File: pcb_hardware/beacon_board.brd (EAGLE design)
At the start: 100 x 38.1 mm, 66 parts, among them IC1-AVR ATMEGA32U4TQFP, J1-ISP AVR_SPI_PRG_6PTH, Q1 PZT2222A, Q2 PZT2222A, Q3 PZT2222A, Q4 PZT2222A, Q5 PZT2222A, Q6 PZT2222A, Q7 PZT2222A, Y1 16MHz

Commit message: Complete alpha prototype for PCB
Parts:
- removed FRAME1: FRAME-LETTER, SparkFun-Aesthetics:CREATIVE_COMMONS
- added R11, R30, R31, R32: 1K, SparkFun-Passives:0805
- moved R5 169.3 mm to (76.2, 12.7), turned to 270 degrees
- moved R4 143.4 mm to (58.4, 29.2)
- moved R3 139.7 mm to (50.8, 11.4), turned to 90 degrees
- moved R2 138.6 mm to (53.3, 11.4), turned to 90 degrees
- moved J1-ISP 129.5 mm to (73.7, 5.08), turned to 180 degrees
- moved C1 129.0 mm to (66.0, 12.7)
- moved C3 127.6 mm to (63.5, 26.7)
- moved JP2-RESET 126.5 mm to (64.8, 3.81), turned to 270 degrees
- moved C5 126.3 mm to (47.0, 11.4)
- moved C2 125.2 mm to (57.1, 11.4)
- moved R1 124.1 mm to (48.3, 26.7), turned to 180 degrees
- moved LOGO1 119.9 mm to (71.1, 34.9)
- moved C4 118.8 mm to (45.7, 17.8), turned to 90 degrees
- moved R27 110.8 mm to (76.2, 34.3), turned to 90 degrees
- moved U$1 90.4 mm to (42.5, 32.8)
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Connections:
- new net N$30: R11.2, R30.2, R31.2, R32.2
- new net N$31: R11.1, R30.1, R31.1, R32.1
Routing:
- net VCC: track 0.00 -> 267.4 mm
- net GND: track 0.00 -> 241.3 mm, vias 0 -> 3
- net N$25: track 0.00 -> 63.0 mm
- net GREEN: track 0.00 -> 58.5 mm
- net N$15: track 0.00 -> 53.6 mm
- net WHITE: track 0.00 -> 35.1 mm
- net D9: track 0.00 -> 34.3 mm
- net D1: track 0.00 -> 34.3 mm
- net RESET: track 0.00 -> 34.2 mm, vias 0 -> 2
- net IR_RX: track 0.00 -> 34.0 mm
- net 38_KHZ_OUT: track 0.00 -> 32.9 mm
- net N$6: track 0.00 -> 32.7 mm
- net D2: track 0.00 -> 31.5 mm
- net MOSI: track 0.00 -> 30.6 mm, vias 0 -> 1
- net N$14: track 0.00 -> 23.4 mm
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- added copper zone on layer 16, net GND
- added copper zone on layer 1, net VCC
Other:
- board text added: "Green"
- board text added: "Junior Design Beacon Board"
- board text added: "R0-8-20-KT"
- board text added: "Red"
- board text added: "White"

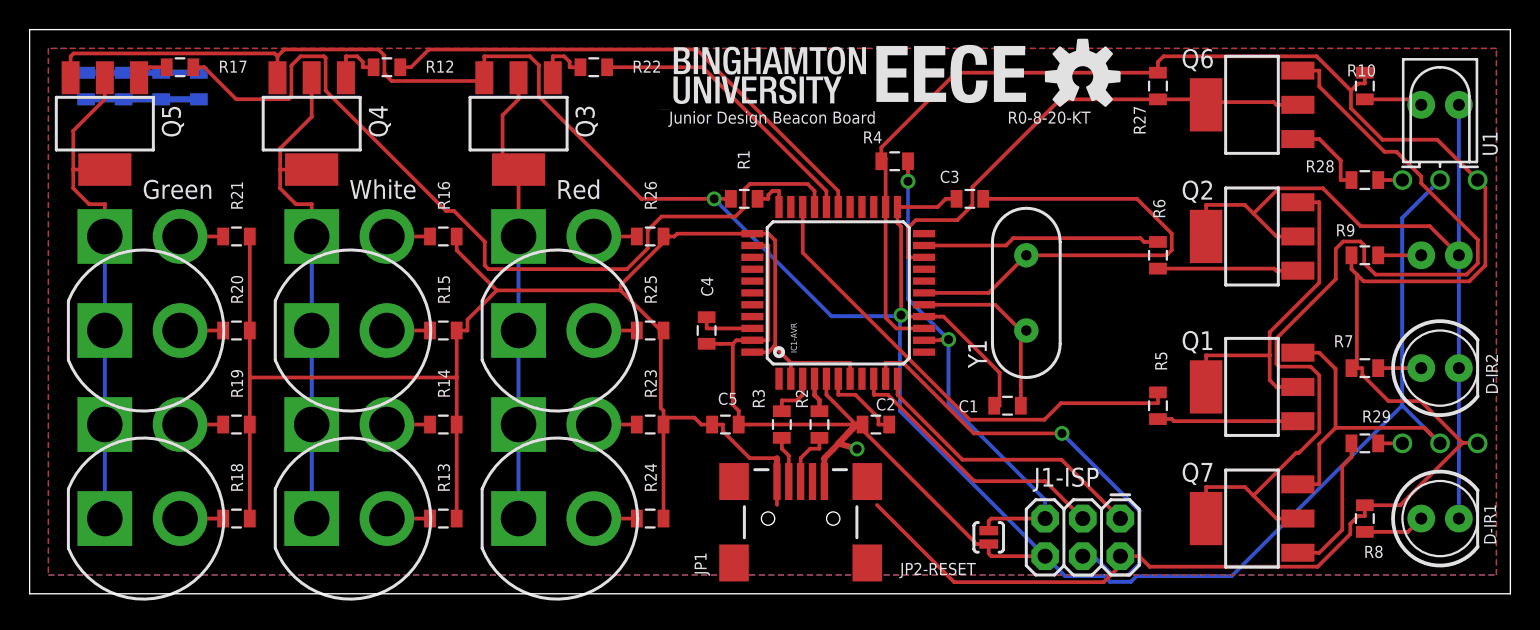
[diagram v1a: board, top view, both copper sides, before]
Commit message: Finish R1 of the beacon board PCB.
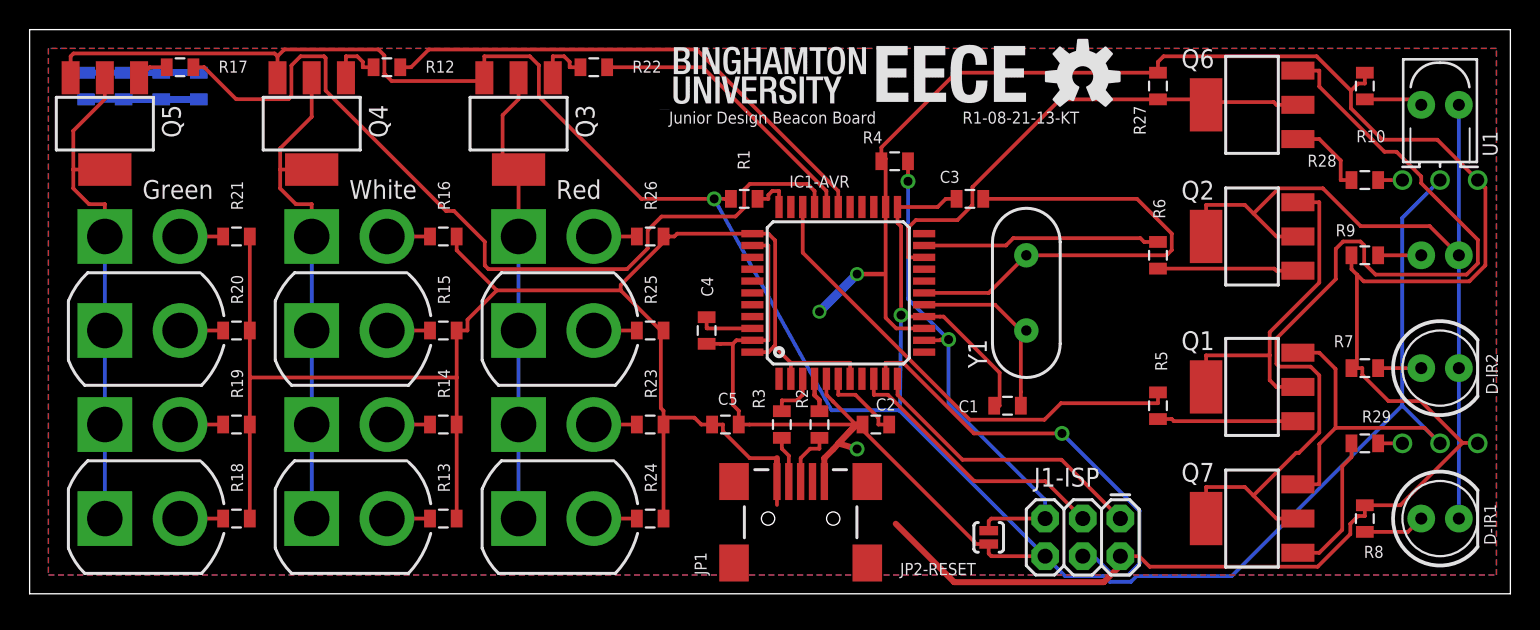
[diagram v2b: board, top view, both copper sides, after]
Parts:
- D1, D10, D11, D12, D2, D3, D4, D5, D6, D7, D8, D9: device SparkFun-LED:LED10MM -> beacon_board:LED10MM
- U1, U2: device junior_design:TSOP382 -> beacon_board:TSOP382
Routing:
- net N$30: track 7.62 -> 28.2 mm
- net N$31: track 7.62 -> 15.2 mm
- net GND: track 241.3 -> 246.4 mm
- net VCC: track 267.4 -> 270.9 mm, vias 0 -> 2
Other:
- board text added: "R1-08-21-13-KT"
- board text removed: "R0-8-20-KT"

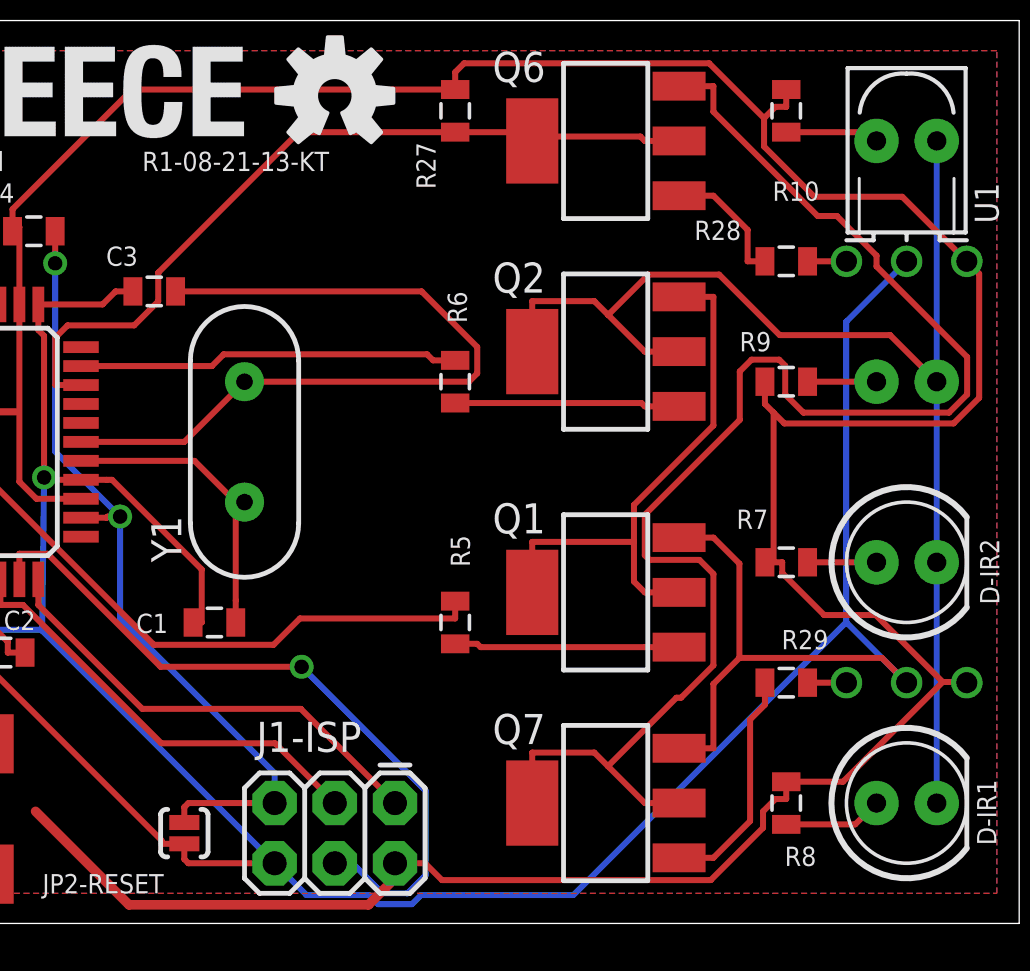
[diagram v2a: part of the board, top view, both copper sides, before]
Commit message: Add parallell resistors for TSOP IR receivers
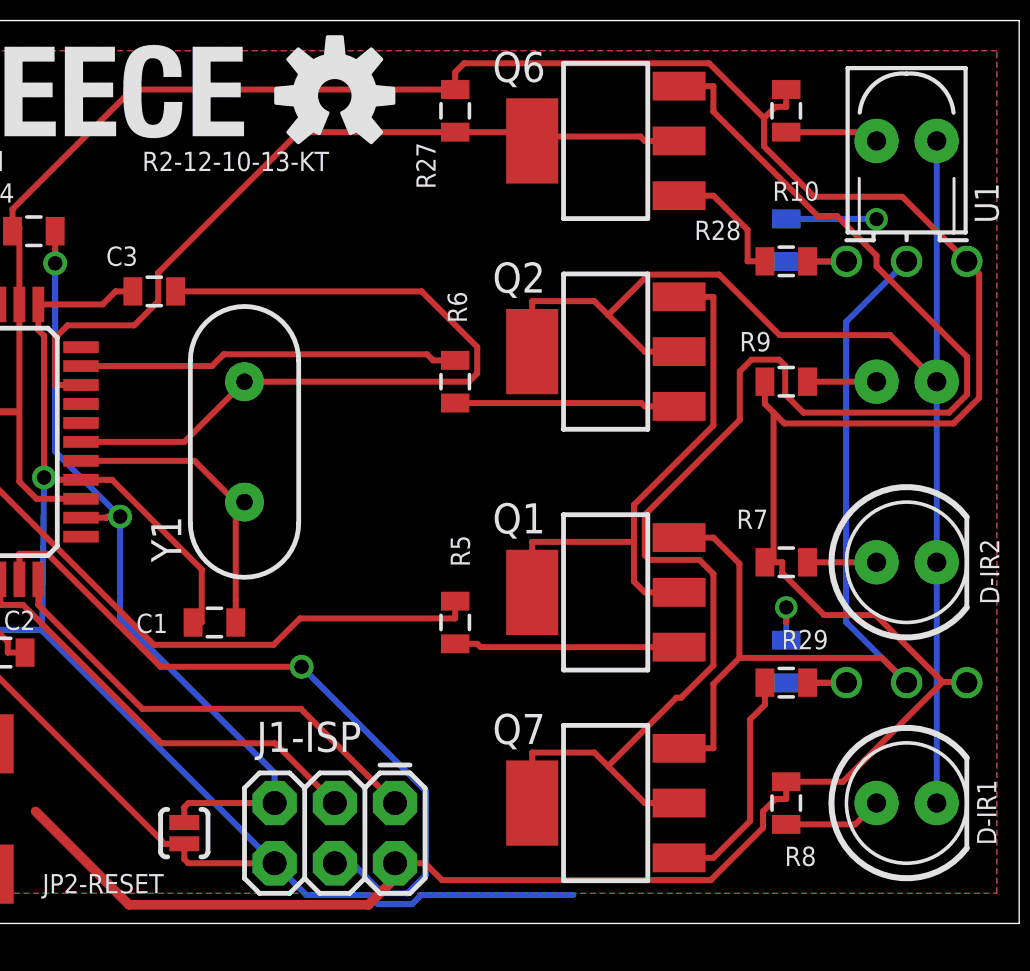
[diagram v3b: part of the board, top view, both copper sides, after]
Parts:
- added R33: 0R, SparkFun-Resistors:0805
- added R34: (no value), SparkFun-Resistors:0805
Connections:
- net N$26: now also R34.2
- net N$29: now also R33.2
- net VCC: now also R33.1, R34.1
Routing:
- net GND: track 246.4 -> 230.1 mm
- net VCC: track 270.9 -> 276.8 mm, vias 2 -> 4
- net N$26: track 1.64 -> 4.19 mm
- net N$29: track 1.64 -> 4.19 mm
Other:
- board text added: "R2-12-10-13-KT"
- board text removed: "R1-08-21-13-KT"
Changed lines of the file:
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@@
 <layer number="27" name="tValues" color="7" fill="1" visible="yes" active="yes"/>
 <layer number="28" name="bValues" color="7" fill="1" visible="yes" active="yes"/>
-<layer number="29" name="tStop" color="7" fill="3" visible="no" active="yes"/>
-<layer number="30" name="bStop" color="7" fill="6" visible="no" active="yes"/>
+<layer number="29" name="tStop" color="7" fill="3" visible="yes" active="yes"/>
+<layer number="30" name="bStop" color="7" fill="6" visible="yes" active="yes"/>
 <layer number="31" name="tCream" color="7" fill="4" visible="no" active="yes"/>
 <layer number="32" name="bCream" color="7" fill="5" visible="no" active="yes"/>
@@
 <layer number="43" name="vRestrict" color="2" fill="10" visible="no" active="yes"/>
 <layer number="44" name="Drills" color="7" fill="1" visible="no" active="yes"/>
-<layer number="45" name="Holes" color="7" fill="1" visible="no" active="yes"/>
+<layer number="45" name="Holes" color="7" fill="1" visible="yes" active="yes"/>
 <layer number="46" name="Milling" color="3" fill="1" visible="no" active="yes"/>
 <layer number="47" name="Measures" color="7" fill="1" visible="no" active="yes"/>
@@
 <wire x1="0" y1="38.1" x2="0" y2="0" width="0" layer="20"/>
 <text x="43.18" y="31.75" size="0.8128" layer="21" font="vector" ratio="15">Junior Design Beacon Board</text>
-<text x="62.992" y="31.75" size="0.8128" layer="21" font="vector" ratio="15">R1-08-21-13-KT</text>
+<text x="62.992" y="31.75" size="0.8128" layer="21" font="vector" ratio="15">R2-12-10-13-KT</text>
 <text x="21.59" y="26.67" size="1.27" layer="25" font="vector" ratio="15">White</text>
 <text x="7.62" y="26.67" size="1.27" layer="25" font="vector" ratio="15">Green</text>
@@
 <pass name="Follow-me" refer="Default" active="yes">
 </pass>
-<pass name="Busses" refer="Default" active="yes">
+<pass name="Busses" refer="Default" active="no">
 <param name="cfNonPref" value="4"/>
 <param name="cfBusImpact" value="4"/>
@@
 <attribute name="NAME" x="2.54" y="32.1945" size="0.8128" layer="26" rot="MR180"/>
 </element>
+<element name="R33" library="SparkFun-Resistors" package="0805" value="0R" x="90.17" y="11.049" rot="MR270"/>
+<element name="R34" library="SparkFun-Resistors" package="0805" value="" x="90.17" y="28.829" rot="MR270"/>
 </elements>
 <signals>
@@
 <wire x1="74.3755" y1="0.8126" x2="74.7617" y2="1.1988" width="0.254" layer="16"/>
 <wire x1="74.7617" y1="1.1988" x2="81.1862" y2="1.1988" width="0.254" layer="16"/>
-<wire x1="81.1862" y1="1.1988" x2="92.6987" y2="12.7113" width="0.254" layer="16"/>
 <wire x1="64.77" y1="3.36" x2="63.8047" y2="3.36" width="0.254" layer="1"/>
 <wire x1="55.8849" y1="11.43" x2="63.8047" y2="3.5102" width="0.254" layer="1"/>
@@
 <wire x1="53.34" y1="19.05" x2="55.88" y2="21.59" width="0.6096" layer="16"/>
 <wire x1="55.88" y1="21.59" x2="57.658" y2="21.59" width="0.3048" layer="1"/>
+<contactref element="R33" pad="1"/>
+<contactref element="R34" pad="1"/>
+<via x="90.17" y="13.335" extent="1-16" drill="0.6"/>
+<wire x1="90.17" y1="13.335" x2="90.17" y2="12.7" width="0.254" layer="1"/>
+<wire x1="90.17" y1="11.949" x2="90.17" y2="13.335" width="0.254" layer="16"/>
+<via x="93.98" y="29.718" extent="1-16" drill="0.6"/>
+<wire x1="90.17" y1="29.729" x2="93.969" y2="29.729" width="0.254" layer="16"/>
+<wire x1="93.969" y1="29.729" x2="93.98" y2="29.718" width="0.254" layer="16"/>
 </signal>
 <signal name="N$5">
@@
 <contactref element="R28" pad="1"/>
 <wire x1="92.71" y1="27.94" x2="91.07" y2="27.94" width="0.254" layer="1"/>
+<contactref element="R34" pad="2"/>
+<wire x1="90.17" y1="27.929" x2="92.71" y2="27.929" width="0.254" layer="16"/>
+<wire x1="92.71" y1="27.929" x2="92.71" y2="27.94" width="0.254" layer="16"/>
 </signal>
 <signal name="N$29">
@@
 <contactref element="R29" pad="1"/>
 <wire x1="92.71" y1="10.16" x2="91.07" y2="10.16" width="0.254" layer="1"/>
+<contactref element="R33" pad="2"/>
+<wire x1="90.17" y1="10.149" x2="92.71" y2="10.149" width="0.254" layer="16"/>
+<wire x1="92.71" y1="10.149" x2="92.71" y2="10.16" width="0.254" layer="16"/>
 </signal>
 <signal name="N$30">
